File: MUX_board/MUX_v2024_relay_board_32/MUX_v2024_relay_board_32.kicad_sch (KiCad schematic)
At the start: 19 parts, among them J1 Relays Pwr, J2 I2C, J3 Screw_Terminal_01x04, J4 Conn_02x08_Odd_Even, J5 Screw_Terminal_01x16, U1 MCP23017_SP, U2 MCP23017_SP

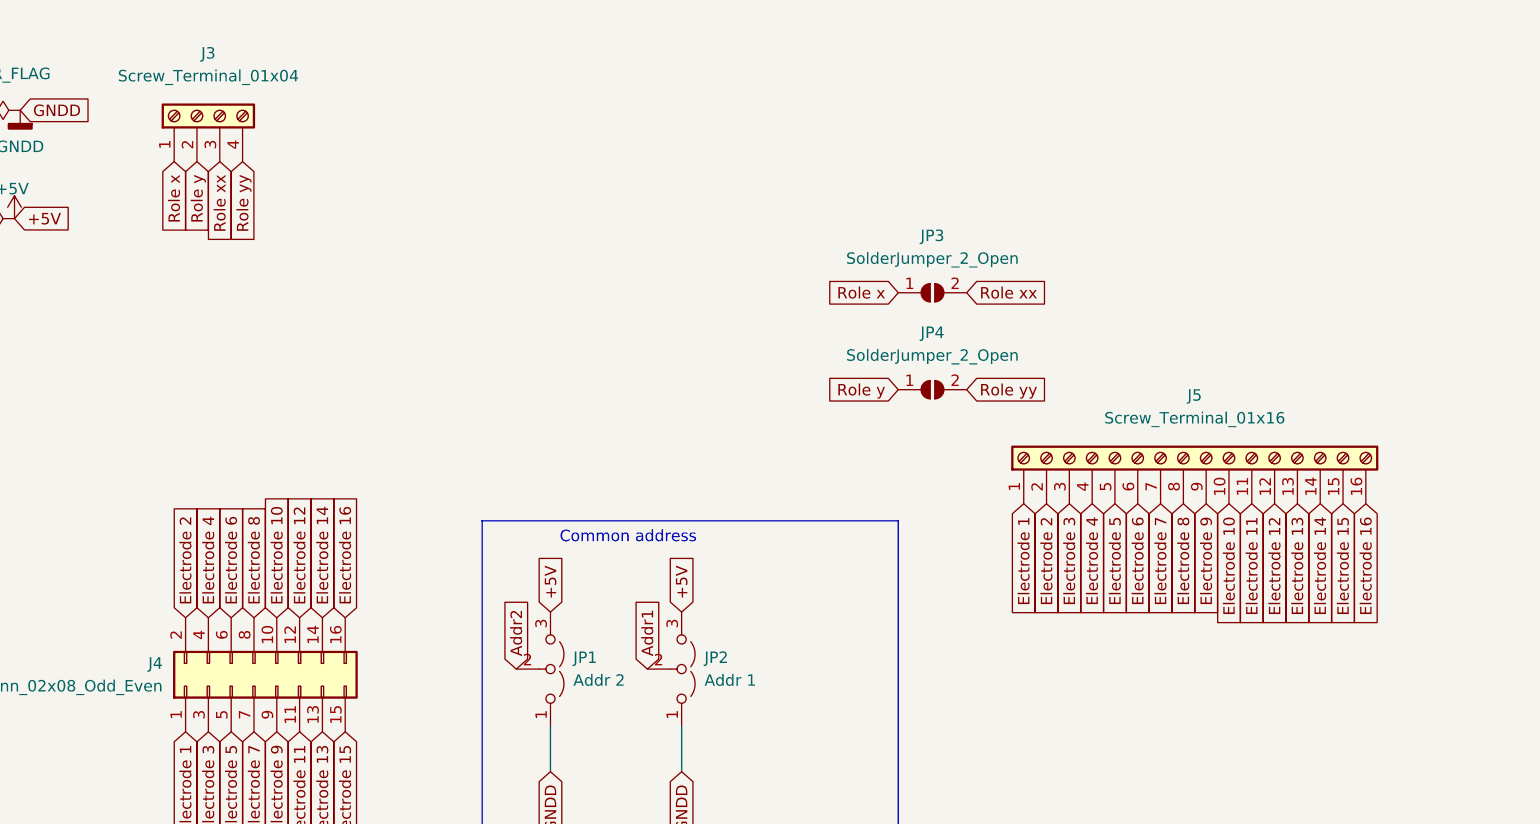
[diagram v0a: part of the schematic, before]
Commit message: Fixes last errors on pcb
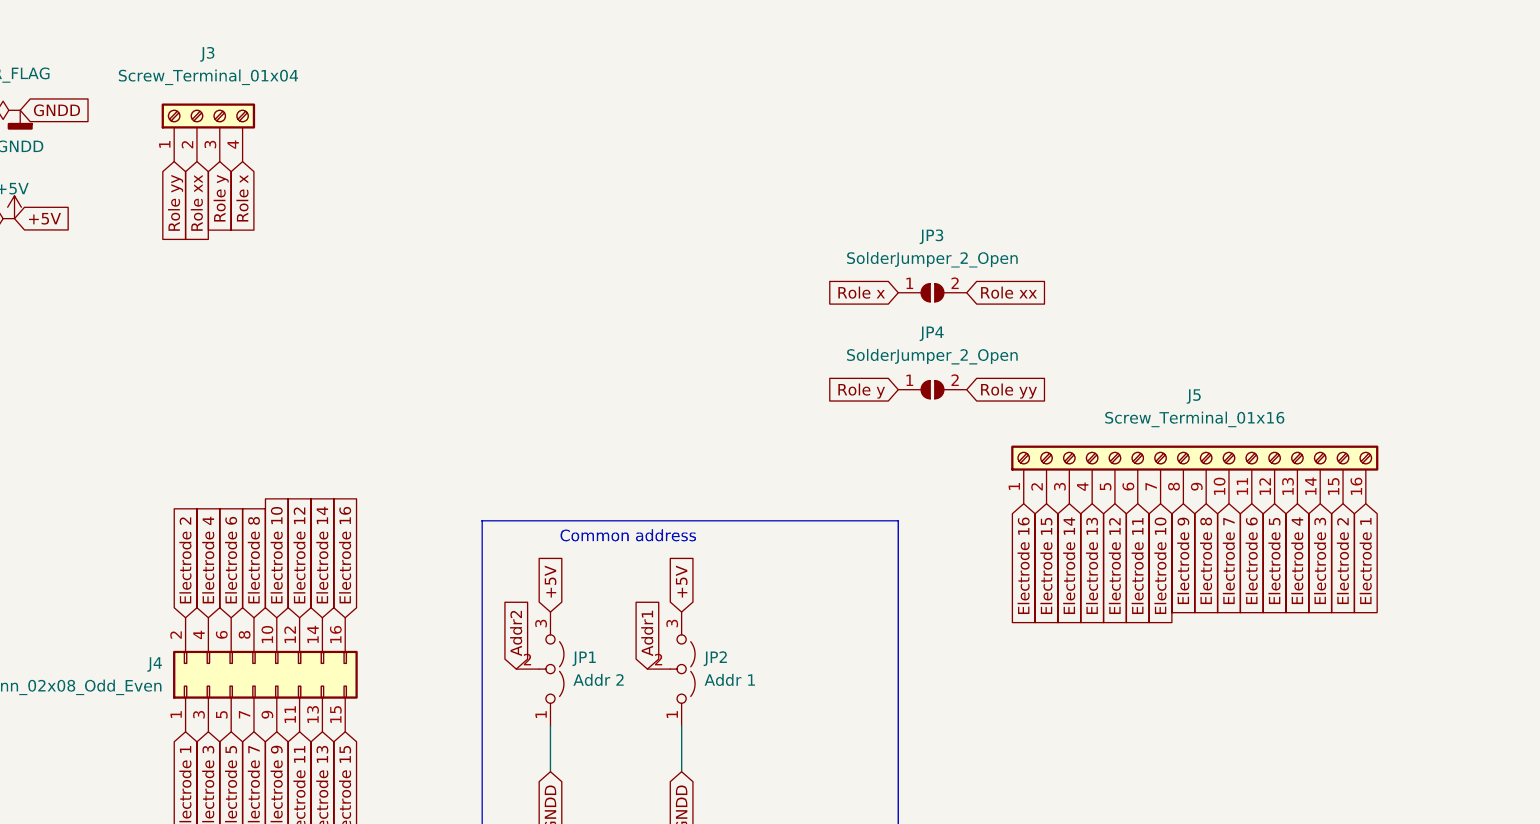
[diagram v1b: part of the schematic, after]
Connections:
- net Electrode 1: now also J5.16 (Pin_16); no longer J5.1 (Pin_1)
- net Electrode 10: now also J5.7 (Pin_7); no longer J5.10 (Pin_10)
- net Electrode 11: now also J5.6 (Pin_6); no longer J5.11 (Pin_11)
- net Electrode 12: now also J5.5 (Pin_5); no longer J5.12 (Pin_12)
- net Electrode 13: now also J5.4 (Pin_4); no longer J5.13 (Pin_13)
- net Electrode 14: now also J5.3 (Pin_3); no longer J5.14 (Pin_14)
- net Electrode 15: now also J5.2 (Pin_2); no longer J5.15 (Pin_15)
- net Electrode 16: now also J5.1 (Pin_1); no longer J5.16 (Pin_16)
- net Electrode 2: now also J5.15 (Pin_15); no longer J5.2 (Pin_2)
- net Electrode 3: now also J5.14 (Pin_14); no longer J5.3 (Pin_3)
- net Electrode 4: now also J5.13 (Pin_13); no longer J5.4 (Pin_4)
- net Electrode 5: now also J5.12 (Pin_12); no longer J5.5 (Pin_5)
- net Electrode 6: now also J5.11 (Pin_11); no longer J5.6 (Pin_6)
- net Electrode 7: now also J5.10 (Pin_10); no longer J5.7 (Pin_7)
- net Electrode 8: now also J5.9 (Pin_9); no longer J5.8 (Pin_8)
- net Electrode 9: now also J5.8 (Pin_8); no longer J5.9 (Pin_9)
- net Role x: now also J3.4 (Pin_4); no longer J3.1 (Pin_1)
- net Role xx: now also J3.2 (Pin_2); no longer J3.3 (Pin_3)
- net Role y: now also J3.3 (Pin_3); no longer J3.2 (Pin_2)
- net Role yy: now also J3.1 (Pin_1); no longer J3.4 (Pin_4)
